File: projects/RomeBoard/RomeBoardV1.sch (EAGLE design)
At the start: 26 parts, among them J1 HEADER-5, J2 RASPBERRY-PI-HEADER, Q1 2N4401, Q2 2N4401, Q3 2N4401

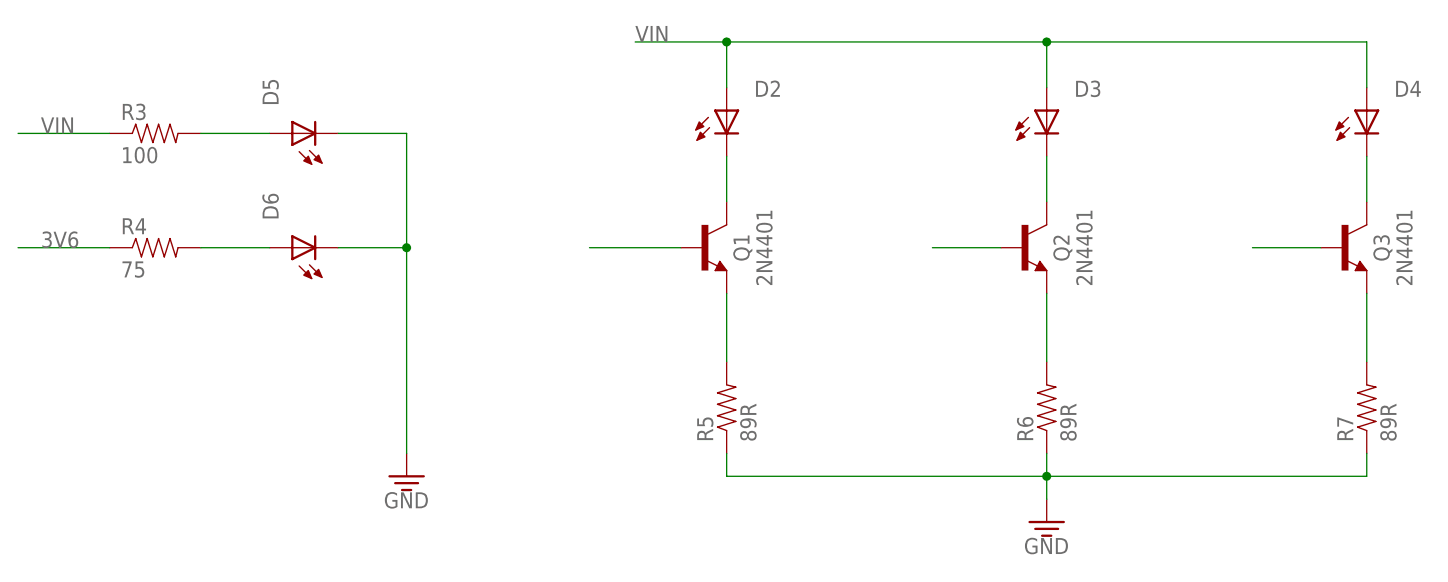
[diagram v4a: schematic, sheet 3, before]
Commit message: NPN -> NMOS
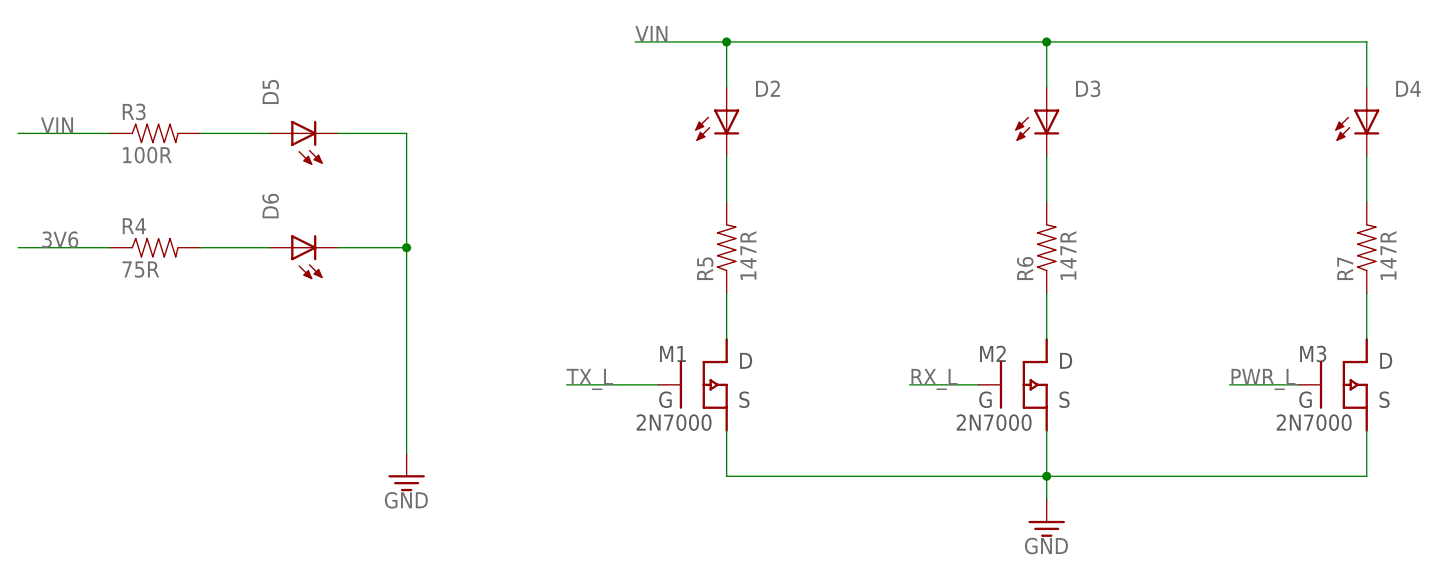
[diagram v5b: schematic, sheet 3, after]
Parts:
- removed Q1, Q2, Q3: 2N4401, BrownSpaceEngineering:2N4401
- added M1, M2, M3: 2N7000, BrownSpaceEngineering:2N7000
- R3: value 100 -> 100R
- R4: value 75 -> 75R
- R5, R6, R7: value 89R -> 147R
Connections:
- net GND: now also M1.S, M2.S, M3.S; no longer R5.1, R6.1, R7.1
- net N$10: now also R5.2; no longer Q1.1
- net N$4: now also R6.2; no longer Q2.1
- net N$5: now also M1.D, R5.1; no longer Q1.3, R5.2
- net N$6: now also M2.D, R6.1; no longer Q2.3, R6.2
- net N$7: now also M3.D, R7.1; no longer Q3.3, R7.2
- net N$9: now also R7.2; no longer Q3.1
- net PWR_L: now also M3.G; no longer Q3.2
- net RX_L: now also M2.G; no longer Q2.2
- net TX_L: now also M1.G; no longer Q1.2
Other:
- moved on the sheet: R5, R6, R7
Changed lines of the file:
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@@
 <part name="D5" library="BrownSpaceEngineering" deviceset="LED" device="THRU-HOLE-CONNECTOR"/>
 <part name="D6" library="BrownSpaceEngineering" deviceset="LED" device="THRU-HOLE-CONNECTOR"/>
-<part name="R3" library="passives" deviceset="RESISTOR" device="-PTH0.4" value="100"/>
-<part name="R4" library="passives" deviceset="RESISTOR" device="-PTH0.4" value="75"/>
+<part name="R3" library="passives" deviceset="RESISTOR" device="-PTH0.4" value="100R"/>
+<part name="R4" library="passives" deviceset="RESISTOR" device="-PTH0.4" value="75R"/>
 <part name="GND5" library="supply1" deviceset="GND" device=""/>
-<part name="Q1" library="BrownSpaceEngineering" deviceset="2N4401" device=""/>
-<part name="Q2" library="BrownSpaceEngineering" deviceset="2N4401" device=""/>
-<part name="Q3" library="BrownSpaceEngineering" deviceset="2N4401" device=""/>
-<part name="R5" library="passives" deviceset="RESISTOR" device="-PTH0.4" value="89R"/>
-<part name="R6" library="passives" deviceset="RESISTOR" device="-PTH0.4" value="89R"/>
-<part name="R7" library="passives" deviceset="RESISTOR" device="-PTH0.4" value="89R"/>
+<part name="R5" library="passives" deviceset="RESISTOR" device="-PTH0.4" value="147R"/>
+<part name="R6" library="passives" deviceset="RESISTOR" device="-PTH0.4" value="147R"/>
+<part name="R7" library="passives" deviceset="RESISTOR" device="-PTH0.4" value="147R"/>
 <part name="GND6" library="supply1" deviceset="GND" device=""/>
+<part name="M1" library="BrownSpaceEngineering" deviceset="2N7000" device=""/>
+<part name="M2" library="BrownSpaceEngineering" deviceset="2N7000" device=""/>
+<part name="M3" library="BrownSpaceEngineering" deviceset="2N7000" device=""/>
 </parts>
 <sheets>
@@
 <attribute name="NAME" x="165.608" y="65.024" size="1.778" layer="95"/>
 </instance>
-<instance part="Q1" gate="G$1" x="88.9" y="48.26"/>
-<instance part="Q2" gate="G$1" x="124.46" y="48.26"/>
-<instance part="Q3" gate="G$1" x="160.02" y="48.26"/>
-<instance part="R5" gate="G$1" x="91.44" y="30.48" rot="R90"/>
-<instance part="R6" gate="G$1" x="127" y="30.48" rot="R90"/>
-<instance part="R7" gate="G$1" x="162.56" y="30.48" rot="R90"/>
+<instance part="R5" gate="G$1" x="91.44" y="48.26" rot="R90"/>
+<instance part="R6" gate="G$1" x="127" y="48.26" rot="R90"/>
+<instance part="R7" gate="G$1" x="162.56" y="48.26" rot="R90"/>
 <instance part="GND6" gate="1" x="127" y="17.78"/>
+<instance part="M1" gate="G$1" x="86.36" y="33.02"/>
+<instance part="M2" gate="G$1" x="121.92" y="33.02"/>
+<instance part="M3" gate="G$1" x="157.48" y="33.02"/>
 </instances>
 <busses>
@@
 </segment>
 <segment>
-<pinref part="R5" gate="G$1" pin="1"/>
-<wire x1="91.44" y1="25.4" x2="91.44" y2="22.86" width="0.1524" layer="91"/>
 <pinref part="GND6" gate="1" pin="GND"/>
 <wire x1="91.44" y1="22.86" x2="127" y2="22.86" width="0.1524" layer="91"/>
 <wire x1="127" y1="22.86" x2="127" y2="20.32" width="0.1524" layer="91"/>
-<pinref part="R6" gate="G$1" pin="1"/>
-<wire x1="127" y1="25.4" x2="127" y2="22.86" width="0.1524" layer="91"/>
 <junction x="127" y="22.86"/>
-<pinref part="R7" gate="G$1" pin="1"/>
 <wire x1="127" y1="22.86" x2="162.56" y2="22.86" width="0.1524" layer="91"/>
-<wire x1="162.56" y1="22.86" x2="162.56" y2="25.4" width="0.1524" layer="91"/>
+<pinref part="M1" gate="G$1" pin="S"/>
+<wire x1="91.44" y1="27.94" x2="91.44" y2="22.86" width="0.1524" layer="91"/>
+<pinref part="M2" gate="G$1" pin="S"/>
+<wire x1="127" y1="27.94" x2="127" y2="22.86" width="0.1524" layer="91"/>
+<pinref part="M3" gate="G$1" pin="S"/>
+<wire x1="162.56" y1="27.94" x2="162.56" y2="22.86" width="0.1524" layer="91"/>
 </segment>
 </net>
@@
 </segment>
 </net>
+<net name="N$9" class="0">
+<segment>
+<pinref part="D4" gate="G$1" pin="C"/>
+<wire x1="162.56" y1="58.42" x2="162.56" y2="53.34" width="0.1524" layer="91"/>
+<pinref part="R7" gate="G$1" pin="2"/>
+</segment>
+</net>
+<net name="N$4" class="0">
+<segment>
+<pinref part="D3" gate="G$1" pin="C"/>
+<wire x1="127" y1="58.42" x2="127" y2="53.34" width="0.1524" layer="91"/>
+<pinref part="R6" gate="G$1" pin="2"/>
+</segment>
+</net>
+<net name="N$10" class="0">
+<segment>
+<pinref part="D2" gate="G$1" pin="C"/>
+<wire x1="91.44" y1="58.42" x2="91.44" y2="53.34" width="0.1524" layer="91"/>
+<pinref part="R5" gate="G$1" pin="2"/>
+</segment>
+</net>
 <net name="N$5" class="0">
 <segment>
-<pinref part="R5" gate="G$1" pin="2"/>
-<pinref part="Q1" gate="G$1" pin="3"/>
-<wire x1="91.44" y1="35.56" x2="91.44" y2="43.18" width="0.1524" layer="91"/>
+<pinref part="M1" gate="G$1" pin="D"/>
+<pinref part="R5" gate="G$1" pin="1"/>
+<wire x1="91.44" y1="38.1" x2="91.44" y2="43.18" width="0.1524" layer="91"/>
 </segment>
 </net>
 <net name="N$6" class="0">
 <segment>
-<pinref part="R6" gate="G$1" pin="2"/>
-<pinref part="Q2" gate="G$1" pin="3"/>
-<wire x1="127" y1="35.56" x2="127" y2="43.18" width="0.1524" layer="91"/>
+<pinref part="R6" gate="G$1" pin="1"/>
+<pinref part="M2" gate="G$1" pin="D"/>
+<wire x1="127" y1="43.18" x2="127" y2="38.1" width="0.1524" layer="91"/>
 </segment>
 </net>
 <net name="N$7" class="0">
 <segment>
-<pinref part="R7" gate="G$1" pin="2"/>
-<pinref part="Q3" gate="G$1" pin="3"/>
-<wire x1="162.56" y1="35.56" x2="162.56" y2="43.18" width="0.1524" layer="91"/>
-</segment>
-</net>
-<net name="N$9" class="0">
-<segment>
-<pinref part="D4" gate="G$1" pin="C"/>
-<pinref part="Q3" gate="G$1" pin="1"/>
-<wire x1="162.56" y1="58.42" x2="162.56" y2="53.34" width="0.1524" layer="91"/>
-</segment>
-</net>
-<net name="N$4" class="0">
-<segment>
-<pinref part="D3" gate="G$1" pin="C"/>
-<pinref part="Q2" gate="G$1" pin="1"/>
-<wire x1="127" y1="58.42" x2="127" y2="53.34" width="0.1524" layer="91"/>
-</segment>
-</net>
-<net name="N$10" class="0">
-<segment>
-<pinref part="D2" gate="G$1" pin="C"/>
-<pinref part="Q1" gate="G$1" pin="1"/>
-<wire x1="91.44" y1="58.42" x2="91.44" y2="53.34" width="0.1524" layer="91"/>
+<pinref part="R7" gate="G$1" pin="1"/>
+<pinref part="M3" gate="G$1" pin="D"/>
+<wire x1="162.56" y1="43.18" x2="162.56" y2="38.1" width="0.1524" layer="91"/>
 </segment>
 </net>
 <net name="TX_L" class="0">
 <segment>
-<pinref part="Q1" gate="G$1" pin="2"/>
-<wire x1="86.36" y1="48.26" x2="76.2" y2="48.26" width="0.1524" layer="91"/>
+<pinref part="M1" gate="G$1" pin="G"/>
+<wire x1="83.82" y1="33.02" x2="73.66" y2="33.02" width="0.1524" layer="91"/>
+<label x="73.66" y="33.02" size="1.778" layer="95"/>
 </segment>
 </net>
 <net name="RX_L" class="0">
 <segment>
-<pinref part="Q2" gate="G$1" pin="2"/>
-<wire x1="121.92" y1="48.26" x2="114.3" y2="48.26" width="0.1524" layer="91"/>
+<pinref part="M2" gate="G$1" pin="G"/>
+<wire x1="119.38" y1="33.02" x2="111.76" y2="33.02" width="0.1524" layer="91"/>
+<label x="111.76" y="33.02" size="1.778" layer="95"/>
 </segment>
 </net>
 <net name="PWR_L" class="0">
 <segment>
-<pinref part="Q3" gate="G$1" pin="2"/>
-<wire x1="157.48" y1="48.26" x2="149.86" y2="48.26" width="0.1524" layer="91"/>
-</segment>
-</net>
+<pinref part="M3" gate="G$1" pin="G"/>
+<wire x1="154.94" y1="33.02" x2="147.32" y2="33.02" width="0.1524" layer="91"/>
+<label x="147.32" y="33.02" size="1.778" layer="95"/>
+</segment>
+</net>
